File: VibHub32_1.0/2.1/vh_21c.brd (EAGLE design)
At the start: 80 x 80 mm, 97 parts, among them Q1 MOSFET_PCH-DMG2305UX-13, Q3 2N7002, U1 DRV8833C, U2 DRV8833C, U3 3.3V, U4 MAX16054AZT+T, U5 CH340C, U6 ESP-WROOM32

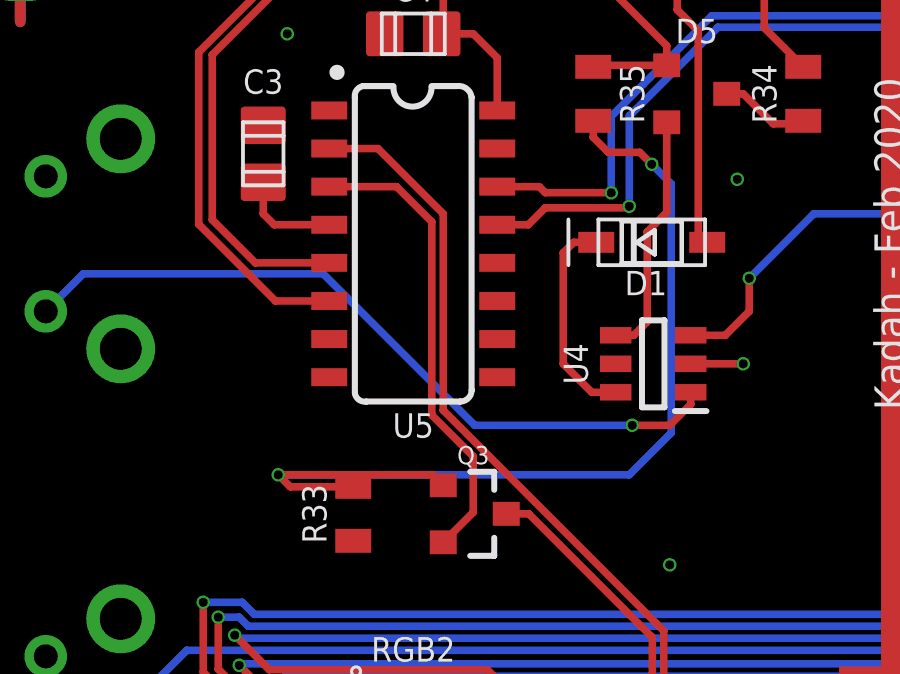
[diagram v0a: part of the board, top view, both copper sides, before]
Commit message: BOM consolidation Removed 150K 0805 res requirement
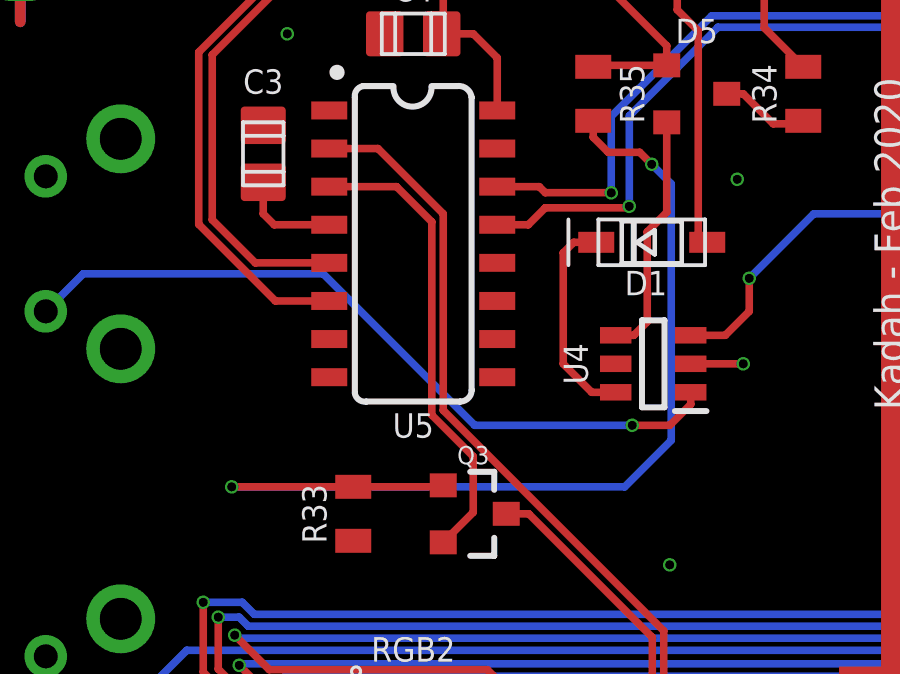
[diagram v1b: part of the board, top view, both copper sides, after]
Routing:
- net N$16: track 34.1 -> 34.7 mm
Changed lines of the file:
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@@
 <wire x1="21.5" y1="59.05" x2="21" y2="59.55" width="0.254" layer="1"/>
 <via x="22.95" y="58.65" extent="1-16" drill="0.3"/>
-<wire x1="23.6" y1="49.7" x2="22.2" y2="48.3" width="0.254" layer="16"/>
-<wire x1="22.2" y1="48.3" x2="10.5" y2="48.3" width="0.254" layer="16"/>
-<via x="10.5" y="48.3" extent="1-16" drill="0.3"/>
-<wire x1="10.5" y1="48.3" x2="15.65" y2="48.3" width="0.254" layer="1"/>
-<wire x1="15.65" y1="48.3" x2="16" y2="47.95" width="0.254" layer="1"/>
+<wire x1="23.6" y1="49.45" x2="22.05" y2="47.9" width="0.254" layer="16"/>
+<wire x1="22.05" y1="47.9" x2="8.95" y2="47.9" width="0.254" layer="16"/>
+<via x="8.95" y="47.9" extent="1-16" drill="0.3"/>
+<wire x1="16" y1="47.95" x2="15.95" y2="47.9" width="0.254" layer="1"/>
+<wire x1="15.95" y1="47.9" x2="13" y2="47.9" width="0.254" layer="1"/>
 <wire x1="22.95" y1="58.65" x2="23.6" y2="58" width="0.254" layer="16"/>
-<wire x1="23.6" y1="58" x2="23.6" y2="49.7" width="0.254" layer="16"/>
-<wire x1="13" y1="47.9" x2="10.9" y2="47.9" width="0.254" layer="1"/>
-<wire x1="10.9" y1="47.9" x2="10.5" y2="48.3" width="0.254" layer="1"/>
+<wire x1="23.6" y1="58" x2="23.6" y2="49.45" width="0.254" layer="16"/>
+<wire x1="13" y1="47.9" x2="8.95" y2="47.9" width="0.254" layer="1"/>
 </signal>
 <signal name="USB_TXD">

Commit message: Unsaved changes from last commit
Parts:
- R33: value 100K -> >1M
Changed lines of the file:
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@@
 <element name="R32" library="vibhud" library_urn="urn:adsk.eagle:library:2530795" package="0805" package3d_urn="urn:adsk.eagle:package:2531030/3" value="&gt;1M" x="34.9" y="67.1" smashed="yes" rot="R90">
 <attribute name="NAME" x="34.011" y="67.1" size="0.8128" layer="25" font="vector" ratio="15" rot="R90" align="bottom-center"/>
-<attribute name="VALUE" x="34.9" y="65.74193125" size="0.8128" layer="27" font="vector" ratio="15" rot="R90" align="center-left"/>
+<attribute name="VALUE" x="35.95" y="67.09193125" size="0.8128" layer="27" font="vector" ratio="15" rot="R90" align="top-center"/>
 </element>
 <element name="U5" library="vibhud" library_urn="urn:adsk.eagle:library:2530795" package="SO016" package3d_urn="urn:adsk.eagle:package:13515173/1" value="CH340C" x="15" y="56" smashed="yes" rot="R270">
@@
 <attribute name="VALUE" x="17" y="45.349" size="0.6096" layer="27" font="vector" ratio="20" align="top-center"/>
 </element>
-<element name="R33" library="vibhud" library_urn="urn:adsk.eagle:library:2530795" package="0805" package3d_urn="urn:adsk.eagle:package:2531030/3" value="100K" x="13" y="47" smashed="yes" rot="R90">
+<element name="R33" library="vibhud" library_urn="urn:adsk.eagle:library:2530795" package="0805" package3d_urn="urn:adsk.eagle:package:2531030/3" value="&gt;1M" x="13" y="47" smashed="yes" rot="R90">
 <attribute name="NAME" x="12.111" y="47" size="0.8128" layer="25" font="vector" ratio="15" rot="R90" align="bottom-center"/>
 <attribute name="VALUE" x="13.889" y="47" size="0.8128" layer="27" font="vector" ratio="10" rot="R90" align="top-center"/>
